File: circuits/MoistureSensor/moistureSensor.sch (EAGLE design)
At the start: 8 parts, among them P1 MCS10B, P2 MCS10B, Q1 BSS84

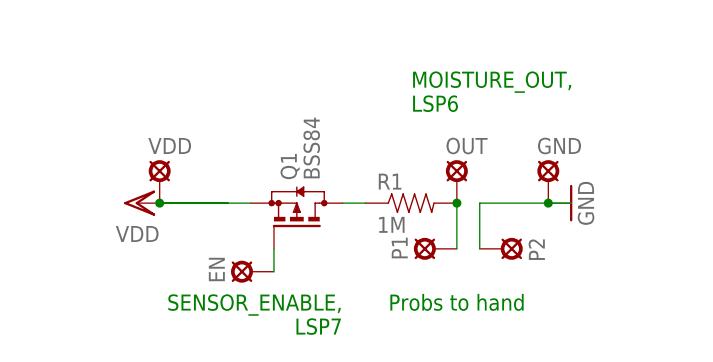
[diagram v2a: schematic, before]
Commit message: Swapped probe and resistor positions
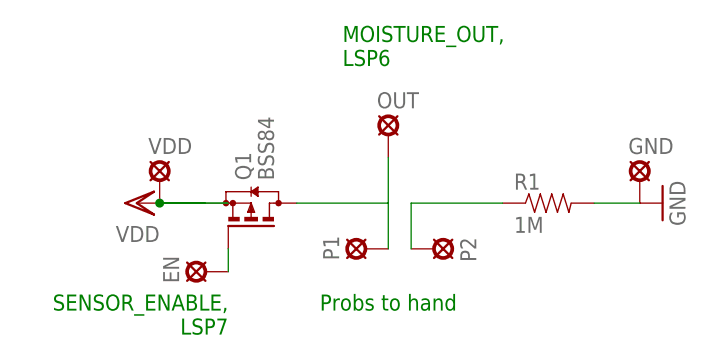
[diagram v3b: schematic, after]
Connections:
- net GND: now also R1.2; no longer P2.MP
- net N$1: now also P2.MP; no longer Q1.D
- net N$3: now also Q1.D; no longer R1.2
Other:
- moved on the sheet: EN, GND, OUT, P1, P2, Q1, R1
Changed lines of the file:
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@@
 <grid distance="0.1" unitdist="inch" unit="inch" style="lines" multiple="1" display="no" altdistance="0.01" altunitdist="inch" altunit="inch"/>
 <layers>
-<layer number="1" name="Top" color="4" fill="1" visible="yes" active="no"/>
-<layer number="16" name="Bottom" color="1" fill="1" visible="yes" active="no"/>
-<layer number="17" name="Pads" color="2" fill="1" visible="yes" active="no"/>
-<layer number="18" name="Vias" color="2" fill="1" visible="yes" active="no"/>
-<layer number="19" name="Unrouted" color="6" fill="1" visible="yes" active="no"/>
-<layer number="20" name="Dimension" color="15" fill="1" visible="yes" active="no"/>
-<layer number="21" name="tPlace" color="7" fill="1" visible="yes" active="no"/>
-<layer number="22" name="bPlace" color="7" fill="1" visible="yes" active="no"/>
-<layer number="23" name="tOrigins" color="15" fill="1" visible="yes" active="no"/>
-<layer number="24" name="bOrigins" color="15" fill="1" visible="yes" active="no"/>
-<layer number="25" name="tNames" color="7" fill="1" visible="yes" active="no"/>
-<layer number="26" name="bNames" color="7" fill="1" visible="yes" active="no"/>
-<layer number="27" name="tValues" color="7" fill="1" visible="yes" active="no"/>
-<layer number="28" name="bValues" color="7" fill="1" visible="yes" active="no"/>
+<layer number="1" name="Top" color="4" fill="1" visible="no" active="no"/>
+<layer number="16" name="Bottom" color="1" fill="1" visible="no" active="no"/>
+<layer number="17" name="Pads" color="2" fill="1" visible="no" active="no"/>
+<layer number="18" name="Vias" color="2" fill="1" visible="no" active="no"/>
+<layer number="19" name="Unrouted" color="6" fill="1" visible="no" active="no"/>
+<layer number="20" name="Dimension" color="15" fill="1" visible="no" active="no"/>
+<layer number="21" name="tPlace" color="7" fill="1" visible="no" active="no"/>
+<layer number="22" name="bPlace" color="7" fill="1" visible="no" active="no"/>
+<layer number="23" name="tOrigins" color="15" fill="1" visible="no" active="no"/>
+<layer number="24" name="bOrigins" color="15" fill="1" visible="no" active="no"/>
+<layer number="25" name="tNames" color="7" fill="1" visible="no" active="no"/>
+<layer number="26" name="bNames" color="7" fill="1" visible="no" active="no"/>
+<layer number="27" name="tValues" color="7" fill="1" visible="no" active="no"/>
+<layer number="28" name="bValues" color="7" fill="1" visible="no" active="no"/>
 <layer number="29" name="tStop" color="7" fill="3" visible="no" active="no"/>
 <layer number="30" name="bStop" color="7" fill="6" visible="no" active="no"/>
@@
 <layer number="35" name="tGlue" color="7" fill="4" visible="no" active="no"/>
 <layer number="36" name="bGlue" color="7" fill="5" visible="no" active="no"/>
-<layer number="37" name="tTest" color="7" fill="1" visible="yes" active="no"/>
-<layer number="38" name="bTest" color="7" fill="1" visible="yes" active="no"/>
+<layer number="37" name="tTest" color="7" fill="1" visible="no" active="no"/>
+<layer number="38" name="bTest" color="7" fill="1" visible="no" active="no"/>
 <layer number="39" name="tKeepout" color="4" fill="11" visible="no" active="no"/>
 <layer number="40" name="bKeepout" color="1" fill="11" visible="no" active="no"/>
@@
 <layer number="44" name="Drills" color="7" fill="1" visible="no" active="no"/>
 <layer number="45" name="Holes" color="7" fill="1" visible="no" active="no"/>
-<layer number="46" name="Milling" color="3" fill="1" visible="yes" active="no"/>
-<layer number="47" name="Measures" color="7" fill="1" visible="yes" active="no"/>
-<layer number="48" name="Document" color="7" fill="1" visible="yes" active="no"/>
-<layer number="49" name="Reference" color="7" fill="1" visible="yes" active="no"/>
-<layer number="50" name="dxf" color="7" fill="1" visible="yes" active="no"/>
-<layer number="51" name="tDocu" color="7" fill="1" visible="yes" active="no"/>
-<layer number="52" name="bDocu" color="7" fill="1" visible="yes" active="no"/>
-<layer number="53" name="tGND_GNDA" color="7" fill="9" visible="yes" active="no"/>
-<layer number="54" name="bGND_GNDA" color="1" fill="9" visible="yes" active="no"/>
-<layer number="56" name="wert" color="7" fill="1" visible="yes" active="no"/>
-<layer number="57" name="tCAD" color="7" fill="1" visible="yes" active="no"/>
+<layer number="46" name="Milling" color="3" fill="1" visible="no" active="no"/>
+<layer number="47" name="Measures" color="7" fill="1" visible="no" active="no"/>
+<layer number="48" name="Document" color="7" fill="1" visible="no" active="no"/>
+<layer number="49" name="Reference" color="7" fill="1" visible="no" active="no"/>
+<layer number="50" name="dxf" color="7" fill="1" visible="no" active="no"/>
+<layer number="51" name="tDocu" color="7" fill="1" visible="no" active="no"/>
+<layer number="52" name="bDocu" color="7" fill="1" visible="no" active="no"/>
+<layer number="53" name="tGND_GNDA" color="7" fill="9" visible="no" active="no"/>
+<layer number="54" name="bGND_GNDA" color="1" fill="9" visible="no" active="no"/>
+<layer number="56" name="wert" color="7" fill="1" visible="no" active="no"/>
+<layer number="57" name="tCAD" color="7" fill="1" visible="no" active="no"/>
 <layer number="90" name="Modules" color="5" fill="1" visible="yes" active="yes"/>
 <layer number="91" name="Nets" color="2" fill="1" visible="yes" active="yes"/>
@@
 </classes>
 <parts>
-<part name="R1" library="SparkFun-Resistors" deviceset="1MOHM-1/10W-1%(0603)" device="" value="1M"/>
 <part name="Q1" library="transistor-small-signal" deviceset="BSS84" device=""/>
 <part name="GND1" library="supply1" deviceset="GND" device=""/>
@@
 <part name="EN" library="solpad" deviceset="MCS10B" device=""/>
 <part name="OUT" library="solpad" deviceset="MCS10B" device=""/>
+<part name="R1" library="SparkFun-Resistors" deviceset="1MOHM-1/10W-1%(0603)" device="" value="1M"/>
 </parts>
 <sheets>
 <sheet>
 <plain>
-<text x="10.16" y="68.58" size="1.778" layer="91">MOISTURE_OUT,
+<text x="2.54" y="73.66" size="1.778" layer="91">MOISTURE_OUT,
 LSP6</text>
-<text x="2.54" y="48.26" size="1.778" layer="91" rot="R180">SENSOR_ENABLE,
+<text x="-10.16" y="48.26" size="1.778" layer="91" rot="R180">SENSOR_ENABLE,
 LSP7</text>
-<text x="22.86" y="48.26" size="1.778" layer="91" rot="R180">Probs to hand</text>
+<text x="15.24" y="48.26" size="1.778" layer="91" rot="R180">Probs to hand</text>
 </plain>
 <instances>
-<instance part="R1" gate="G$1" x="10.16" y="58.42"/>
-<instance part="Q1" gate="G$1" x="-2.54" y="58.42" rot="R90"/>
-<instance part="GND1" gate="1" x="27.94" y="58.42" rot="R90"/>
+<instance part="Q1" gate="G$1" x="-7.62" y="58.42" rot="R90"/>
+<instance part="GND1" gate="1" x="38.1" y="58.42" rot="R90"/>
 <instance part="VDD1" gate="G$1" x="-20.32" y="58.42" rot="R90"/>
-<instance part="P1" gate="1" x="12.7" y="53.34" rot="R90"/>
-<instance part="P2" gate="1" x="20.32" y="53.34" rot="R270"/>
-<instance part="GND" gate="1" x="25.4" y="60.96"/>
+<instance part="P1" gate="1" x="5.08" y="53.34" rot="R90"/>
+<instance part="P2" gate="1" x="12.7" y="53.34" rot="R270"/>
+<instance part="GND" gate="1" x="35.56" y="60.96"/>
 <instance part="VDD" gate="1" x="-17.78" y="60.96"/>
-<instance part="EN" gate="1" x="-7.62" y="50.8" rot="R90"/>
-<instance part="OUT" gate="1" x="15.24" y="60.96"/>
+<instance part="EN" gate="1" x="-12.7" y="50.8" rot="R90"/>
+<instance part="OUT" gate="1" x="7.62" y="66.04"/>
+<instance part="R1" gate="G$1" x="25.4" y="58.42"/>
 </instances>
 <busses>
 </busses>
 <nets>
-<net name="N$1" class="0">
-<segment>
-<pinref part="R1" gate="G$1" pin="1"/>
+<net name="N$3" class="0">
+<segment>
+<pinref part="P1" gate="1" pin="MP"/>
+<wire x1="7.62" y1="63.5" x2="7.62" y2="58.42" width="0.1524" layer="91"/>
+<pinref part="OUT" gate="1" pin="MP"/>
 <pinref part="Q1" gate="G$1" pin="D"/>
-<wire x1="5.08" y1="58.42" x2="2.54" y2="58.42" width="0.1524" layer="91"/>
-</segment>
-</net>
-<net name="N$3" class="0">
-<segment>
+<wire x1="7.62" y1="58.42" x2="7.62" y2="53.34" width="0.1524" layer="91"/>
+<wire x1="-2.54" y1="58.42" x2="7.62" y2="58.42" width="0.1524" layer="91"/>
+</segment>
+</net>
+<net name="GND" class="0">
+<segment>
+<pinref part="GND1" gate="1" pin="GND"/>
+<pinref part="GND" gate="1" pin="MP"/>
 <pinref part="R1" gate="G$1" pin="2"/>
-<pinref part="P1" gate="1" pin="MP"/>
-<wire x1="15.24" y1="58.42" x2="15.24" y2="53.34" width="0.1524" layer="91"/>
-<pinref part="OUT" gate="1" pin="MP"/>
-<junction x="15.24" y="58.42"/>
-</segment>
-</net>
-<net name="GND" class="0">
-<segment>
-<wire x1="17.78" y1="58.42" x2="25.4" y2="58.42" width="0.1524" layer="91"/>
-<pinref part="GND1" gate="1" pin="GND"/>
-<wire x1="25.4" y1="58.42" x2="27.94" y2="58.42" width="0.1524" layer="91"/>
-<junction x="25.4" y="58.42"/>
-<pinref part="P2" gate="1" pin="MP"/>
-<wire x1="17.78" y1="58.42" x2="17.78" y2="53.34" width="0.1524" layer="91"/>
-<pinref part="GND" gate="1" pin="MP"/>
+<wire x1="30.48" y1="58.42" x2="35.56" y2="58.42" width="0.1524" layer="91"/>
 </segment>
 </net>
@@
 <pinref part="VDD1" gate="G$1" pin="VDD"/>
 <junction x="-17.78" y="58.42"/>
-<wire x1="-17.78" y1="58.42" x2="-7.62" y2="58.42" width="0.1524" layer="91"/>
+<wire x1="-17.78" y1="58.42" x2="-12.7" y2="58.42" width="0.1524" layer="91"/>
 <pinref part="VDD" gate="1" pin="MP"/>
 </segment>
@@
 <pinref part="EN" gate="1" pin="MP"/>
 <pinref part="Q1" gate="G$1" pin="G"/>
-<wire x1="-5.08" y1="50.8" x2="-5.08" y2="53.34" width="0.1524" layer="91"/>
-</segment>
-</net>
+<wire x1="-10.16" y1="50.8" x2="-10.16" y2="53.34" width="0.1524" layer="91"/>
+</segment>
+</net>
+<net name="N$1" class="0">
+<segment>
+<pinref part="P2" gate="1" pin="MP"/>
+<wire x1="10.16" y1="53.34" x2="10.16" y2="58.42" width="0.1524" layer="91"/>
+<wire x1="10.16" y1="58.42" x2="20.32" y2="58.42" width="0.1524" layer="91"/>
+<pinref part="R1" gate="G$1" pin="1"/>
+</segment>
+</net>
